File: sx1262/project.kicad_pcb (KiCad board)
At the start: 2 copper layers, 25.4 x 21.9 mm, 7 parts, among them J1 Conn_01x08_Female, J2 Conn_01x02_Female, U1 nicerf-lora-sx1262

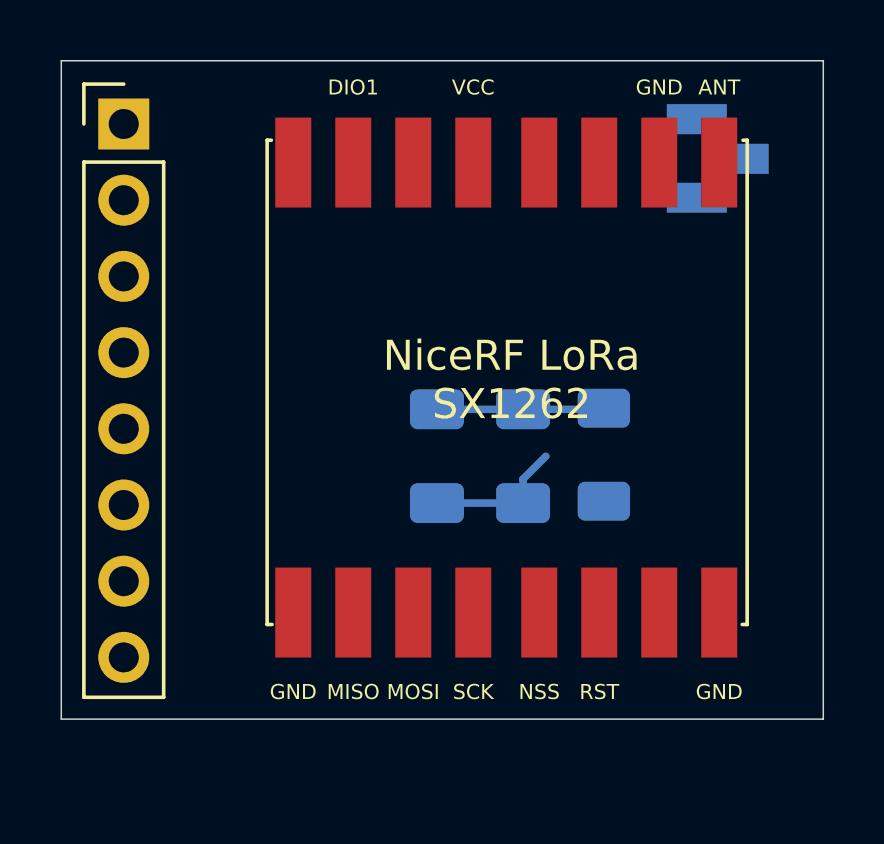
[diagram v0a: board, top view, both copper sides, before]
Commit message: Added dual-channel RF adapter
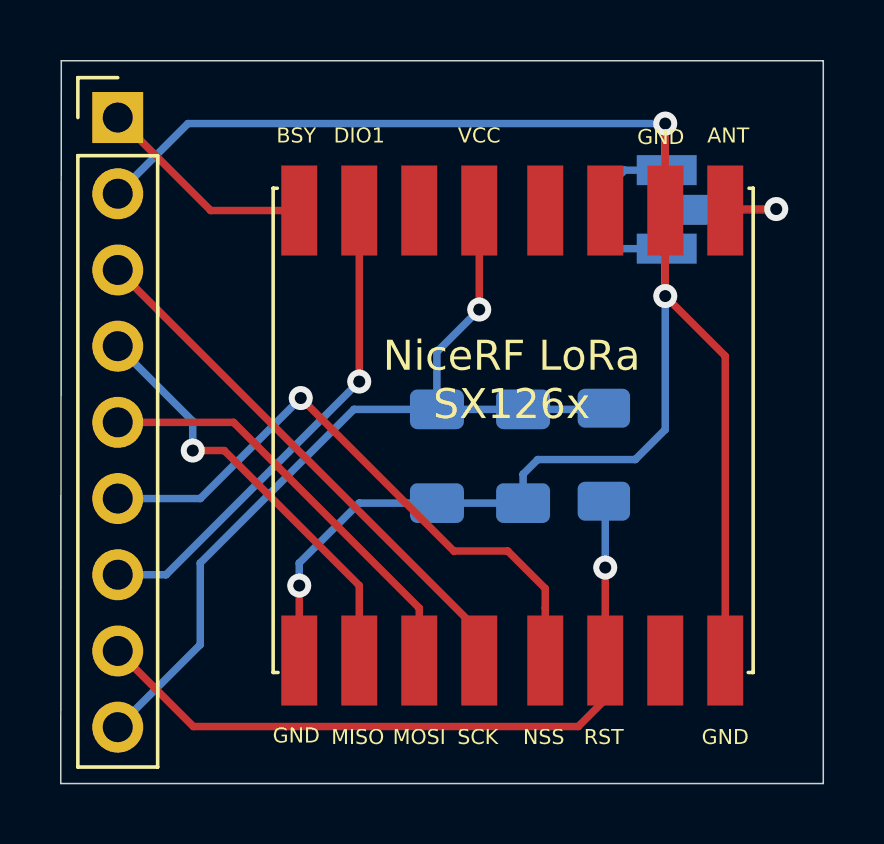
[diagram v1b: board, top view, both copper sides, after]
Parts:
- J1: value Conn_01x08_Female -> Conn_01x09_Female; footprint Connector_PinHeader_2.54mm:PinHeader_1x08_P2.54mm_Vertical -> Connector_PinHeader_2.54mm:PinHeader_1x09_P2.54mm_Vertical
- moved J2 1.97 mm to (138.8, 64.1)
- moved U1 1.61 mm to (134.2, 70.2)
- moved J1 0.29 mm to (120.5, 61.0)
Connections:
- J1 pad 1: /GND -> /BUSY
- J1 pad 2: /SCK -> /GND
- J1 pad 3: /MISO -> /SCK
- J1 pad 4: /MOSI -> /MISO
- J1 pad 5: /NSS -> /MOSI
- J1 pad 6: /DIO0 -> /NSS
- J1 pad 7: /RESET -> /DIO0
- J1 pad 8: /VCC -> /RESET
- U1 pad 16: Net-(U1-Pad16) -> /BUSY
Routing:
- net /GND: track 4.75 -> 69.5 mm, vias 0 -> 3
- net /RESET: track 0.00 -> 24.3 mm, vias 0 -> 1
- net /VCC: track 5.58 -> 29.4 mm, vias 0 -> 1
- net /NSS: track 0.00 -> 20.7 mm, vias 0 -> 1
- net /SCK: track 0.00 -> 18.0 mm
- net /DIO0: track 0.00 -> 16.4 mm, vias 0 -> 1
- net /MISO: track 0.00 -> 14.4 mm, vias 0 -> 1
- net /MOSI: track 0.00 -> 14.4 mm
- net /BUSY: track 0.00 -> 7.33 mm
- net /ANT: track 0.00 -> 3.98 mm, vias 0 -> 1
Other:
- board size 25.4 x 21.9 mm -> 25.4 x 24.1 mm
- board text added: "BSY"
- board text added: "BUSY"
- board text added: "NiceRF LoRa SX126x"
- board text added: "NiceRF SX126x breakout (c) 2021 dushin.net v0.1.0-beta1"
- board text removed: "NiceRF LoRa SX1262"
- board text removed: "NiceRF SX1262 breakout (c) 2021 dushin.net v0.1.0-beta1"
- board text removed: "RESET"
